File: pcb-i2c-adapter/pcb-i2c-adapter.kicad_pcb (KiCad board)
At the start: 2 copper layers, 35 x 30 mm, 9 parts, among them J1 Conn_01x09_Male, J2 Grove, J3 Conn_01x04_Male, J4 Conn_01x04_Male, J5 Conn_01x09_Male

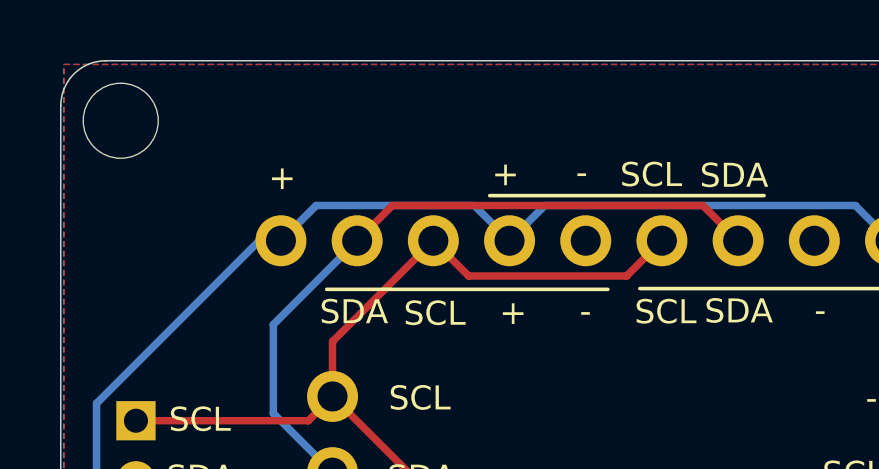
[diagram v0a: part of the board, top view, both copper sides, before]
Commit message: added label for Pi-pinout
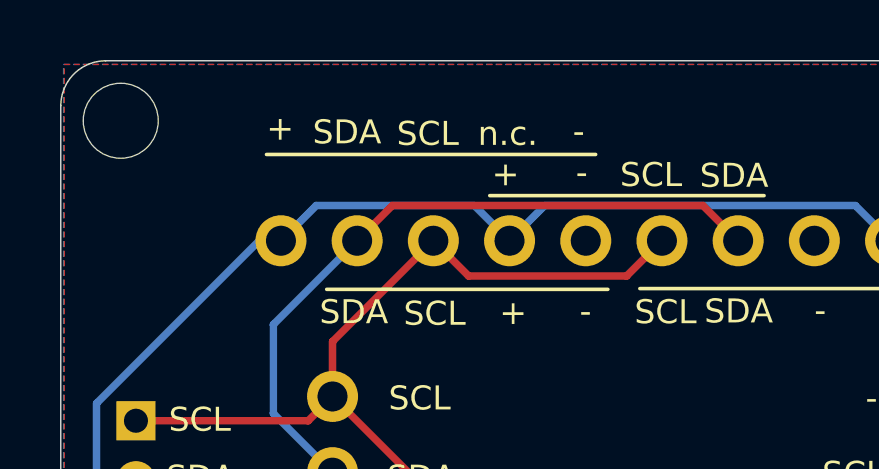
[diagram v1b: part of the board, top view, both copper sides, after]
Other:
- board text added: "n.c."
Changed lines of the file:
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@@
   (general
     (thickness 1.6)
-    (drawings 100)
+    (drawings 105)
     (tracks 56)
     (zones 0)
@@
     (pad 1 np_thru_hole circle (at 0 0) (size 2.5 2.5) (drill 2.5) (layers *.Cu *.Mask))
   )
+  (gr_text n.c. (at 114.902 102.4344) (layer F.SilkS)
+    (effects (font (size 0.8 0.8) (thickness 0.15)))
+  )
+  (gr_text SCL (at 112.235 102.4344) (layer F.SilkS)
+    (effects (font (size 0.8 0.8) (thickness 0.15)))
+  )
+  (gr_line (start 106.8578 103.124) (end 117.8306 103.124) (layer F.SilkS) (width 0.12))
+  (gr_text - (at 117.2642 102.3582) (layer F.SilkS)
+    (effects (font (size 0.8 0.8) (thickness 0.15)))
+  )
+  (gr_text SDA (at 109.5426 102.3836) (layer F.SilkS)
+    (effects (font (size 0.8 0.8) (thickness 0.15)))
+  )
   (gr_text "Rev: 2" (at 109.9058 128.397) (layer B.SilkS)
     (effects (font (size 1 1) (thickness 0.15)) (justify left mirror))
@@
     (effects (font (size 0.8 0.8) (thickness 0.15)) (justify left mirror))
   )
-  (gr_text + (at 107.3836 103.9076) (layer F.SilkS)
-    (effects (font (size 0.8 0.8) (thickness 0.15)))
-  )
+  (gr_text + (at 107.315 102.2604) (layer F.SilkS)
+    (effects (font (size 0.8 0.8) (thickness 0.15)))
+  )
